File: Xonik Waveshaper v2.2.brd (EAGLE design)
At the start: 55.9 x 23.2 mm, 97 parts, among them IC1 TL074JT, IC2 TL074JT, IC3 TL074JT, IC4 TL072JT, IC5 4013T, IC6 LM311T, T1 2n3904

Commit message: Cleaned up and error checked
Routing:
- net GND: track 42.6 -> 43.2 mm
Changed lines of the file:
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@@
 <setting verticaltext="up"/>
 </settings>
-<grid distance="12.5" unitdist="mil" unit="mil" style="lines" multiple="1" display="yes" altdistance="0.025" altunitdist="inch" altunit="inch"/>
+<grid distance="6.25" unitdist="mil" unit="mil" style="lines" multiple="1" display="yes" altdistance="0.025" altunitdist="inch" altunit="inch"/>
 <layers>
 <layer number="1" name="Top" color="4" fill="1" visible="yes" active="yes"/>
@@
 </element>
 <element name="7" library="rcl" library_urn="urn:adsk.eagle:library:334" package="R0603" package3d_urn="urn:adsk.eagle:package:23555/3" value="100k" x="2.2225" y="16.1925" smashed="yes">
-<attribute name="NAME" x="0.3175" y="15.875" size="0.8128" layer="25" font="vector"/>
+<attribute name="NAME" x="1.905" y="15.5575" size="0.8128" layer="25" font="vector" rot="R270"/>
 <attribute name="POPULARITY" value="70" x="2.2225" y="16.1925" size="1.778" layer="27" display="off"/>
 <attribute name="SPICEPREFIX" value="R" x="2.2225" y="16.1925" size="1.778" layer="27" display="off"/>
@@
 </element>
 <element name="8" library="rcl" library_urn="urn:adsk.eagle:library:334" package="R0603" package3d_urn="urn:adsk.eagle:package:23555/3" value="200k" x="2.2225" y="13.97" smashed="yes" rot="R180">
-<attribute name="NAME" x="0.9525" y="14.2875" size="0.8128" layer="25" font="vector" rot="R180"/>
+<attribute name="NAME" x="1.905" y="13.335" size="0.8128" layer="25" font="vector" rot="R270"/>
 <attribute name="POPULARITY" value="70" x="2.2225" y="13.97" size="1.778" layer="27" rot="R180" display="off"/>
 <attribute name="SPICEPREFIX" value="R" x="2.2225" y="13.97" size="1.778" layer="27" rot="R180" display="off"/>
@@
 </element>
 <element name="15" library="rcl" library_urn="urn:adsk.eagle:library:334" package="R0603" package3d_urn="urn:adsk.eagle:package:23555/3" value="50k" x="15.24" y="20.32" smashed="yes" rot="R90">
-<attribute name="NAME" x="14.605" y="21.9075" size="0.8128" layer="25" font="vector"/>
+<attribute name="NAME" x="14.605" y="22.06625" size="0.8128" layer="25" font="vector"/>
 <attribute name="POPULARITY" value="70" x="15.24" y="20.32" size="1.778" layer="27" rot="R90" display="off"/>
 <attribute name="SPICEPREFIX" value="R" x="15.24" y="20.32" size="1.778" layer="27" rot="R90" display="off"/>
@@
 </element>
 <element name="C1" library="joakim" package="R0603-J" value="10pF" x="41.11625" y="7.62" smashed="yes" rot="R270">
-<attribute name="NAME" x="41.8465" y="5.93725" size="0.8128" layer="25" font="vector" rot="R180"/>
+<attribute name="NAME" x="42.00525" y="6.096" size="0.8128" layer="25" font="vector" rot="R180"/>
 <attribute name="VALUE" x="39.08425" y="8.509" size="1.27" layer="27" rot="R270"/>
 </element>
@@
 </element>
 <element name="C3" library="joakim" package="R0603-J" value="30pF" x="27.46375" y="16.8275" smashed="yes" rot="R270">
-<attribute name="NAME" x="26.7335" y="14.38275" size="0.8128" layer="25" font="vector"/>
+<attribute name="NAME" x="26.7335" y="14.224" size="0.8128" layer="25" font="vector"/>
 <attribute name="VALUE" x="25.43175" y="17.7165" size="1.27" layer="27" rot="R270"/>
 </element>
 <element name="C4" library="joakim" package="R0603-J" value="30pF" x="27.46375" y="11.1125" smashed="yes" rot="R90">
-<attribute name="NAME" x="26.7335" y="12.79525" size="0.8128" layer="25" font="vector"/>
+<attribute name="NAME" x="28.194" y="13.716" size="0.8128" layer="25" font="vector" rot="R180"/>
 <attribute name="VALUE" x="29.49575" y="10.2235" size="1.27" layer="27" rot="R90"/>
 </element>
@@
 </element>
 <element name="D1" library="joakim" package="D0805-J" value="1N41480805" x="10.795" y="20.32" smashed="yes" rot="R270">
-<attribute name="NAME" x="10.3505" y="22.2885" size="0.8128" layer="25" font="vector"/>
+<attribute name="NAME" x="10.19175" y="22.12975" size="0.8128" layer="25" font="vector"/>
 <attribute name="VALUE" x="8.509" y="21.082" size="1.27" layer="27" rot="R270"/>
 </element>
 <element name="D2" library="joakim" package="D0805-J" value="1N41480805" x="13.0175" y="20.32" smashed="yes" rot="R270">
-<attribute name="NAME" x="12.573" y="22.2885" size="0.8128" layer="25" font="vector"/>
+<attribute name="NAME" x="12.41425" y="22.12975" size="0.8128" layer="25" font="vector"/>
 <attribute name="VALUE" x="10.7315" y="21.082" size="1.27" layer="27" rot="R270"/>
 </element>
@@
 <wire x1="6.35" y1="8.39875" x2="6.35" y2="7.62" width="0.254" layer="1"/>
 <via x="6.35" y="7.62" extent="1-16" drill="0.3302"/>
-<wire x1="0.9525" y1="20.0025" x2="0.9525" y2="20.4675" width="0.254" layer="1"/>
+<wire x1="0.9525" y1="19.3675" x2="0.9525" y2="20.4675" width="0.254" layer="1"/>
 <wire x1="0.955" y1="20.4675" x2="0.9525" y2="20.4675" width="0.254" layer="1"/>
-<via x="0.9525" y="20.0025" extent="1-16" drill="0.3302"/>
+<via x="0.9525" y="19.3675" extent="1-16" drill="0.3302"/>
 <wire x1="6.35" y1="19.54125" x2="6.35" y2="20.32" width="0.254" layer="1"/>
 <via x="6.35" y="20.32" extent="1-16" drill="0.3302"/>

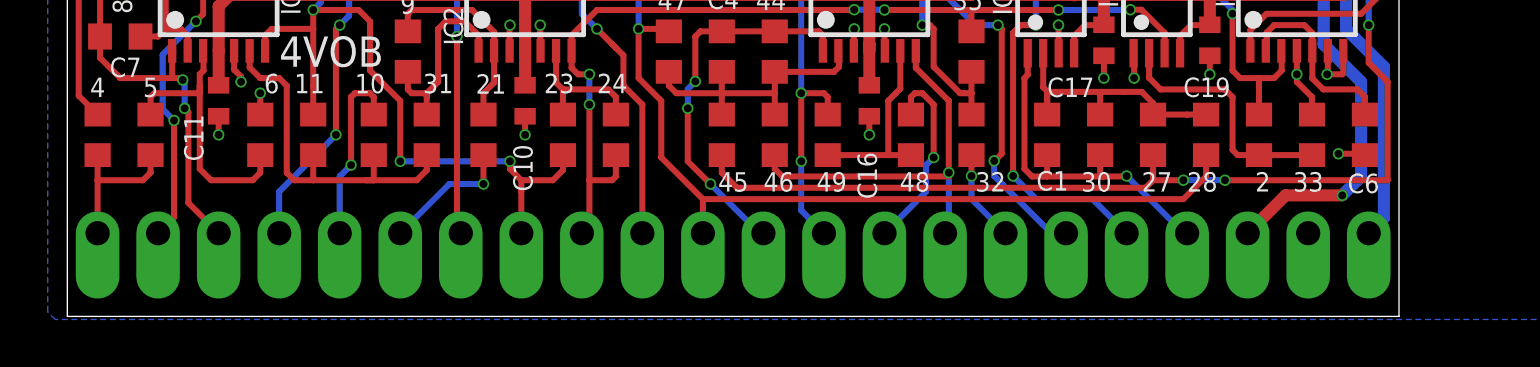
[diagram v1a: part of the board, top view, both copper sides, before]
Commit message: Changed waveshaper to -5V
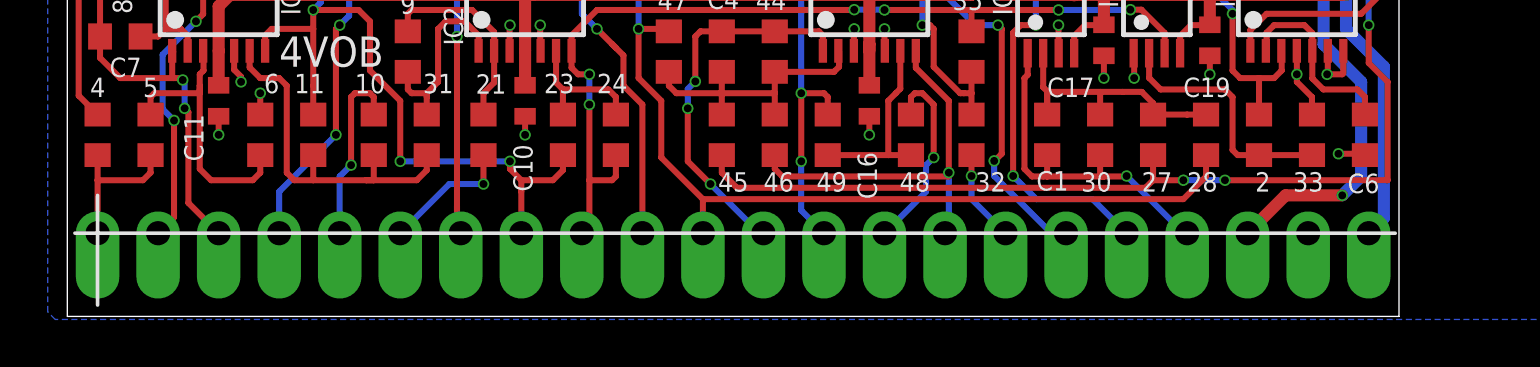
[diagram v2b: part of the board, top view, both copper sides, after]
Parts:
- 25, 28: value 10k -> 20k
- 39, 47: value 49.9k -> 100k
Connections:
- net -2.5V renamed -5V
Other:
- board text added: "-5V"
- board text removed: "-2.5V"
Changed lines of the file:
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@@
 <grid distance="6.25" unitdist="mil" unit="mil" style="lines" multiple="1" display="yes" altdistance="0.025" altunitdist="inch" altunit="inch"/>
 <layers>
-<layer number="1" name="Top" color="4" fill="1" visible="yes" active="yes"/>
+<layer number="1" name="Top" color="4" fill="1" visible="no" active="yes"/>
 <layer number="2" name="Route2" color="1" fill="3" visible="no" active="no"/>
 <layer number="3" name="Route3" color="4" fill="3" visible="no" active="no"/>
 <layer number="14" name="Route14" color="1" fill="6" visible="no" active="no"/>
 <layer number="15" name="Route15" color="4" fill="6" visible="no" active="no"/>
-<layer number="16" name="Bottom" color="1" fill="1" visible="no" active="yes"/>
+<layer number="16" name="Bottom" color="1" fill="1" visible="yes" active="yes"/>
 <layer number="17" name="Pads" color="2" fill="1" visible="yes" active="yes"/>
 <layer number="18" name="Vias" color="2" fill="1" visible="yes" active="yes"/>
 <layer number="19" name="Unrouted" color="6" fill="1" visible="no" active="yes"/>
 <layer number="20" name="Dimension" color="15" fill="1" visible="yes" active="yes"/>
-<layer number="21" name="tPlace" color="7" fill="1" visible="yes" active="yes"/>
+<layer number="21" name="tPlace" color="7" fill="1" visible="no" active="yes"/>
 <layer number="22" name="bPlace" color="7" fill="1" visible="no" active="yes"/>
-<layer number="23" name="tOrigins" color="15" fill="1" visible="yes" active="yes"/>
-<layer number="24" name="bOrigins" color="15" fill="1" visible="no" active="yes"/>
-<layer number="25" name="tNames" color="7" fill="1" visible="yes" active="yes"/>
-<layer number="26" name="bNames" color="7" fill="1" visible="no" active="yes"/>
+<layer number="23" name="tOrigins" color="15" fill="1" visible="no" active="yes"/>
+<layer number="24" name="bOrigins" color="15" fill="1" visible="yes" active="yes"/>
+<layer number="25" name="tNames" color="7" fill="1" visible="no" active="yes"/>
+<layer number="26" name="bNames" color="7" fill="1" visible="yes" active="yes"/>
 <layer number="27" name="tValues" color="7" fill="1" visible="no" active="yes"/>
 <layer number="28" name="bValues" color="7" fill="1" visible="no" active="yes"/>
@@
 <layer number="37" name="tTest" color="7" fill="1" visible="no" active="yes"/>
 <layer number="38" name="bTest" color="7" fill="1" visible="no" active="yes"/>
-<layer number="39" name="tKeepout" color="4" fill="11" visible="yes" active="yes"/>
+<layer number="39" name="tKeepout" color="4" fill="11" visible="no" active="yes"/>
 <layer number="40" name="bKeepout" color="1" fill="11" visible="no" active="yes"/>
 <layer number="41" name="tRestrict" color="4" fill="10" visible="no" active="yes"/>
@@
 <layer number="49" name="Reference" color="7" fill="1" visible="no" active="yes"/>
 <layer number="50" name="dxf" color="7" fill="1" visible="no" active="no"/>
-<layer number="51" name="tDocu" color="7" fill="1" visible="yes" active="yes"/>
+<layer number="51" name="tDocu" color="7" fill="1" visible="no" active="yes"/>
 <layer number="52" name="bDocu" color="7" fill="1" visible="no" active="yes"/>
 <layer number="53" name="tGND_GNDA" color="7" fill="9" visible="no" active="no"/>
@@
 <text x="18.415" y="5.715" size="1.016" layer="26" font="vector" rot="MR90">Saw inv</text>
 <text x="20.955" y="5.715" size="1.016" layer="26" font="vector" rot="MR90">Saw</text>
-<text x="25.9715" y="5.715" size="1.016" layer="26" font="vector" rot="MR90">-2.5V</text>
+<text x="25.9715" y="5.715" size="1.016" layer="26" font="vector" rot="MR90">-5V</text>
 <text x="23.495" y="5.715" size="1.016" layer="26" font="vector" rot="MR90">Sine</text>
 <text x="31.3055" y="5.715" size="1.016" layer="26" font="vector" rot="MR90">Saw 1</text>
@@
 <text x="15.875" y="5.715" size="1.016" layer="26" font="vector" rot="MR90">Triangle</text>
 <text x="8.89" y="10.4775" size="1.27" layer="25" font="vector">4VOB</text>
+<wire x1="0.3175" y1="3.4925" x2="55.72125" y2="3.4925" width="0.1524" layer="25"/>
+<wire x1="1.27" y1="5.08" x2="1.27" y2="0.47625" width="0.1524" layer="25"/>
 </plain>
 <attributes>
@@
 <attribute name="VALUE" x="21.11375" y="8.255" size="1.27" layer="27" rot="R270"/>
 </element>
-<element name="25" library="rcl" library_urn="urn:adsk.eagle:library:334" package="R0603" package3d_urn="urn:adsk.eagle:package:23555/3" value="10k" x="37.62375" y="20.32" smashed="yes" rot="R90">
+<element name="25" library="rcl" library_urn="urn:adsk.eagle:library:334" package="R0603" package3d_urn="urn:adsk.eagle:package:23555/3" value="20k" x="37.62375" y="20.32" smashed="yes" rot="R90">
 <attribute name="NAME" x="36.83" y="22.06625" size="0.8128" layer="25" font="vector"/>
 <attribute name="POPULARITY" value="70" x="37.62375" y="20.32" size="1.778" layer="27" rot="R90" display="off"/>
@@
 <attribute name="VALUE" x="47.46625" y="6.985" size="1.27" layer="27" rot="R90"/>
 </element>
-<element name="28" library="rcl" library_urn="urn:adsk.eagle:library:334" package="R0603" package3d_urn="urn:adsk.eagle:package:23555/3" value="10k" x="47.78375" y="7.62" smashed="yes" rot="R90">
+<element name="28" library="rcl" library_urn="urn:adsk.eagle:library:334" package="R0603" package3d_urn="urn:adsk.eagle:package:23555/3" value="20k" x="47.78375" y="7.62" smashed="yes" rot="R90">
 <attribute name="NAME" x="46.99" y="5.23875" size="0.8128" layer="25" font="vector"/>
 <attribute name="POPULARITY" value="70" x="47.78375" y="7.62" size="1.778" layer="27" rot="R90" display="off"/>
@@
 <attribute name="VALUE" x="33.49625" y="20.955" size="1.27" layer="27" rot="R270"/>
 </element>
-<element name="39" library="rcl" library_urn="urn:adsk.eagle:library:334" package="R0603" package3d_urn="urn:adsk.eagle:package:23555/3" value="49.9k" x="25.24125" y="16.8275" smashed="yes" rot="R270">
+<element name="39" library="rcl" library_urn="urn:adsk.eagle:library:334" package="R0603" package3d_urn="urn:adsk.eagle:package:23555/3" value="100k" x="25.24125" y="16.8275" smashed="yes" rot="R270">
 <attribute name="NAME" x="26.035" y="15.08125" size="0.8128" layer="25" font="vector" rot="R180"/>
 <attribute name="POPULARITY" value="70" x="25.24125" y="16.8275" size="1.778" layer="27" rot="R270" display="off"/>
@@
 <attribute name="VALUE" x="27.78125" y="8.255" size="1.27" layer="27" rot="R270"/>
 </element>
-<element name="47" library="rcl" library_urn="urn:adsk.eagle:library:334" package="R0603" package3d_urn="urn:adsk.eagle:package:23555/3" value="49.9k" x="25.24125" y="11.1125" smashed="yes" rot="R90">
+<element name="47" library="rcl" library_urn="urn:adsk.eagle:library:334" package="R0603" package3d_urn="urn:adsk.eagle:package:23555/3" value="100k" x="25.24125" y="11.1125" smashed="yes" rot="R90">
 <attribute name="NAME" x="24.765" y="12.85875" size="0.8128" layer="25" font="vector"/>
 <attribute name="POPULARITY" value="70" x="25.24125" y="11.1125" size="1.778" layer="27" rot="R90" display="off"/>
@@
 <wire x1="30.7975" y1="6.50875" x2="30.7975" y2="4.445" width="0.254" layer="16"/>
 </signal>
-<signal name="-2.5V">
+<signal name="-5V">
 <contactref element="25" pad="1"/>
 <contactref element="28" pad="1"/>

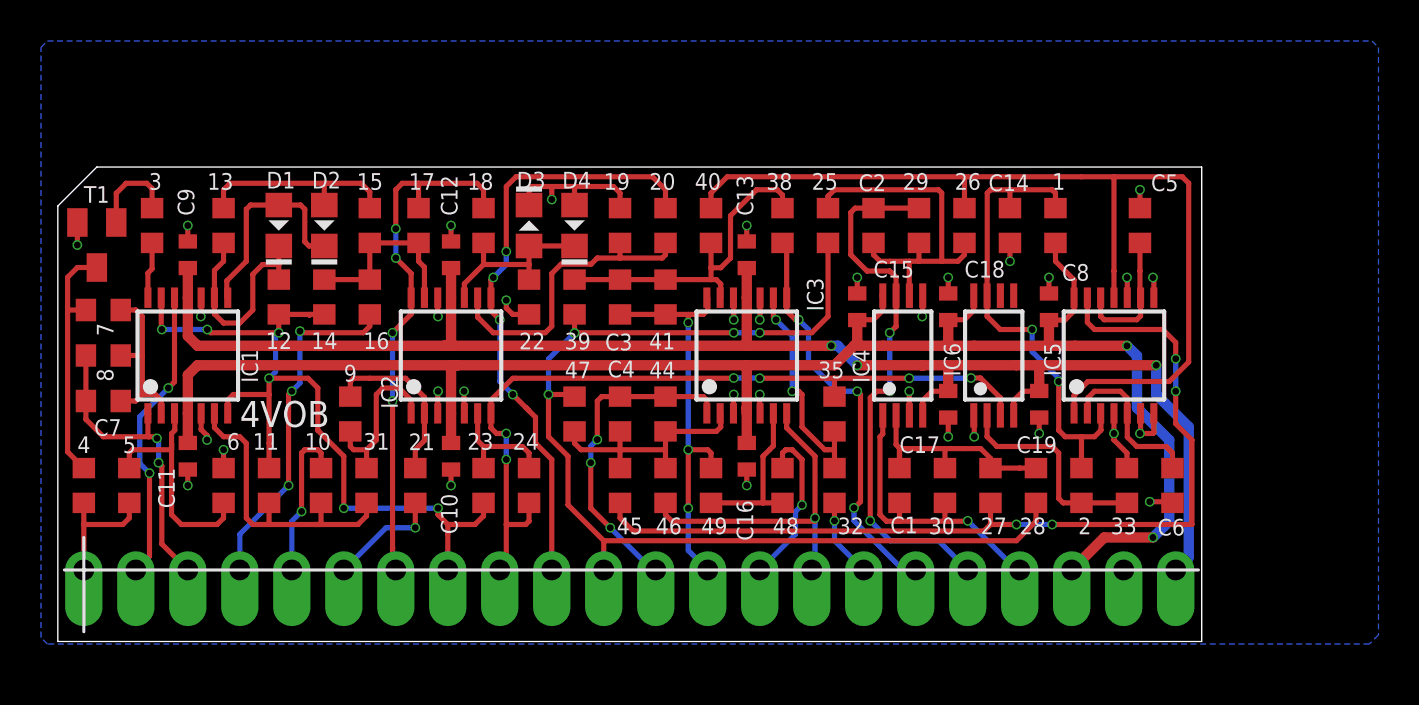
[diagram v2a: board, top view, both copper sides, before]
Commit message: Changed pins to smaller ones
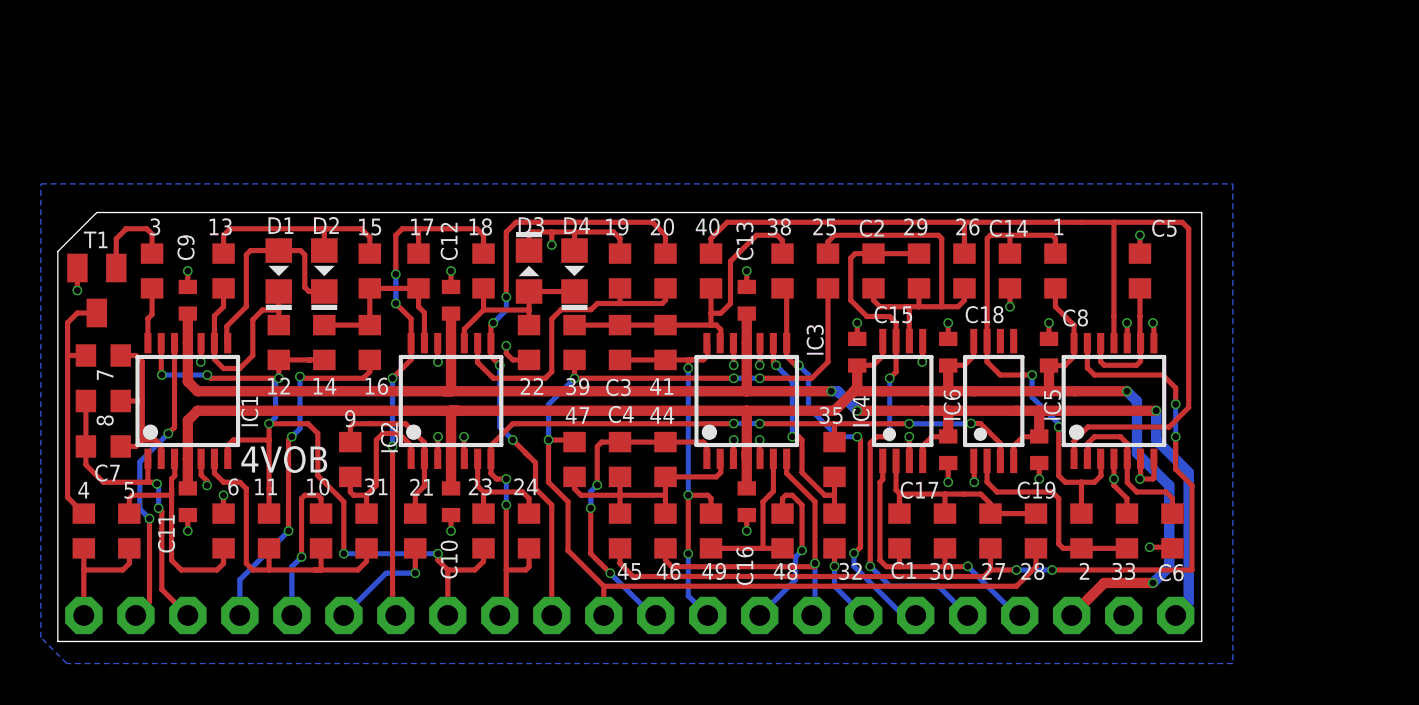
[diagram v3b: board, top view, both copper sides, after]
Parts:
- +12V, -12V, -2.5V, DCO_IN, GND, INV_SAW, IN_CENTER, PULSE, PULSE_AMP_CV, PW_CV, SAW, SINE, ST1, ST2, ST3, ST4, SUB_SAW_1, SUB_SAW_2, SUB_SQR_1, SUB_SQR_2, SYMMETRY, TRIANGLE: device joakim:SIP-PIN01-1J -> joakim:MA01N-1J
- moved +12V 2.22 mm to (49.5, 1.27)
- moved -12V 2.22 mm to (54.6, 1.27)
- moved -2.5V 2.22 mm to (26.7, 1.27)
- moved 1 2.22 mm to (48.7, 18.1)
- moved 10 2.22 mm to (12.9, 5.40)
- moved 11 2.22 mm to (10.3, 5.40)
- moved 12 2.22 mm to (10.8, 14.6)
- moved 13 2.22 mm to (8.10, 18.1)
- moved 14 2.22 mm to (13.0, 14.6)
- moved 15 2.22 mm to (15.2, 18.1)
- moved 16 2.22 mm to (15.2, 14.6)
- moved 17 2.22 mm to (17.6, 18.1)
- moved 18 2.22 mm to (20.8, 18.1)
- moved 19 2.22 mm to (27.5, 18.1)
- moved 2 2.22 mm to (50.0, 5.40)
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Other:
- board size 55.9 x 23.2 mm -> 55.9 x 21 mm

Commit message: Updated with bipolar pwm
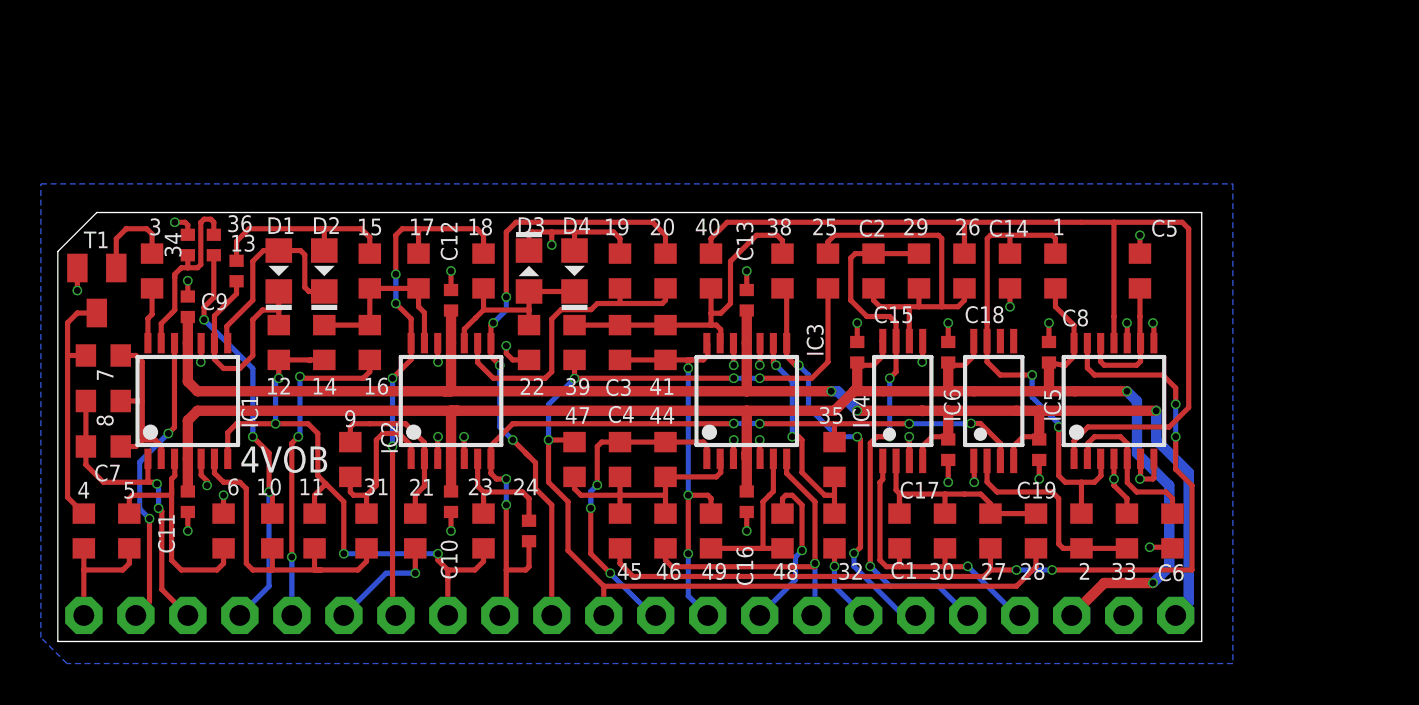
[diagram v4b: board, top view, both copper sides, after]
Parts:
- added 34, 36: 100k, rcl:R0402
- 13, 24: device rcl:R0603 -> rcl:R0402
- C10, C11, C12, C13, C15, C16, C17, C18, C19, C8, C9: device rcl:C0402 -> joakim:C0402-J
- moved DCO_IN 2.54 mm to (8.89, 1.27)
- moved SYMMETRY 2.54 mm to (11.4, 1.27)
- moved 10 2.38 mm to (10.5, 5.40)
- moved 11 2.22 mm to (12.5, 5.40)
- moved 13 0.63 mm to (8.73, 18.1)
- moved C9 0.32 mm to (6.35, 16.4)
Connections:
- new net N$8: 34.1, 36.2, IC1.13
- net DCO_IN: now also 36.1
- net GND: now also 34.2
- net INV_SAW: no longer IC1.13
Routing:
- net DCO_IN: track 7.73 -> 20.8 mm, vias 1 -> 3
- net INV_SAW: track 39.5 -> 30.0 mm, vias 6 -> 4
- net N$8: track 0.00 -> 9.15 mm
- net GND: track 43.2 -> 45.9 mm, vias 34 -> 35
- net +12V: track 86.7 -> 88.1 mm
- net SYMMETRY: track 17.0 -> 16.0 mm
- net -12V: track 76.9 -> 77.7 mm
- net N$11: track 10.8 -> 11.4 mm
